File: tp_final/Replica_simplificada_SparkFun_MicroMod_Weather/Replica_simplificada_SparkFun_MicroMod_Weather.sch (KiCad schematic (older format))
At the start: 33 parts, among them J1 USB_C_Receptacle_USB2.0, J2 Conn_01x05, J3 Conn_01x02, J4 Conn_01x03, J5 Conn_01x03, U1 BME280, U2 AP7361C-33F, U3 AS3935

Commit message: PCB revision 1 listo
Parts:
- removed J5: Conn_01x03, Connector_PinSocket_2.54mm:PinSocket_1x03_P2.54mm_Vertical, symbol Connector_Generic:Conn_01x03
- removed U3: AS3935, Package_DFN_QFN:MLPQ-16-1EP_4x4mm_P0.65mm_EP2.8x2.8mm, symbol Sensor:AS3935
- added U3: AS3935, Package_DFN_QFN:MLPQ-16-1EP_4x4mm_P0.65mm_EP2.8x2.8mm, symbol Sensor_lightning:AS3935
- C11: renamed from 0.22u1; value C -> 0.22u
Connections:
- net labels removed: USB_D+, USB_D-, VBUS
- wire segments 121 -> 115
- no-connect marks 7 -> 9
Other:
- moved on the sheet: J3
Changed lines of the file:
@@
 	0    -1   -1   0
-$EndComp
-$Comp
-L Sensor:AS3935 U3
-U 1 1 60618699
-P 3450 3800
-F 0 "U3" H 3450 3900 50  0000 C CNN
-F 1 "AS3935" H 3100 4250 50  0000 C CNN
-F 2 "Package_DFN_QFN:MLPQ-16-1EP_4x4mm_P0.65mm_EP2.8x2.8mm" H 4250 4700 50  0001 C CNN
-F 3 "http://www.embeddedadventures.com/datasheets/AS3935_Datasheet_EN_v2.pdf" H 3350 3800 50  0001 C CNN
-	1    3450 3800
-	1    0    0    -1
 $EndComp
 Text Notes 1200 2500 0    50   ~ 10
 Regulador de tension
 NoConn ~ 4250 8550
-$Comp
-L power:VBUS #PWR021
-U 1 1 6063B3B4
-P 7200 2900
-F 0 "#PWR021" H 7200 2750 50  0001 C CNN
-F 1 "VBUS" H 7215 3073 50  0000 C CNN
-F 2 "" H 7200 2900 50  0001 C CNN
-F 3 "" H 7200 2900 50  0001 C CNN
-	1    7200 2900
-	1    0    0    -1
-$EndComp
 Wire Wire Line
 	7200 2900 7200 2950
@@
 Wire Wire Line
 	7900 3150 7700 3150
-Text GLabel 7100 3650 2    50   BiDi ~ 0
-USB_D+
-Text GLabel 7100 3550 2    50   BiDi ~ 0
-USB_D-
-Wire Wire Line
-	7100 3550 7000 3550
-Wire Wire Line
-	7100 3650 7000 3650
 Wire Notes Line
 	5850 2550 5850 4800
@@
 $EndComp
 $Comp
-L Device:C 0.22u1
+L Device:C C11
 U 1 1 60613459
 P 4200 1250
-F 0 "0.22u1" H 4315 1296 50  0000 L CNN
-F 1 "C" H 4315 1205 50  0000 L CNN
+F 0 "C11" H 4315 1296 50  0000 L CNN
+F 1 "0.22u" H 4315 1205 50  0000 L CNN
 F 2 "Capacitor_SMD:C_1206_3216Metric" H 4238 1100 50  0001 C CNN
 F 3 "~" H 4200 1250 50  0001 C CNN
@@
 F 3 "~" H 5000 3800 50  0001 C CNN
 	1    5000 3800
-	1    0    0    -1
+	1    0    0    1
 $EndComp
 $Comp
@@
 $EndComp
 $Comp
-L Connector_Generic:Conn_01x03 J5
-U 1 1 60825316
-P 8000 4300
-F 0 "J5" H 8080 4342 50  0000 L CNN
-F 1 "Conn_01x03" H 8080 4251 50  0000 L CNN
-F 2 "Connector_PinSocket_2.54mm:PinSocket_1x03_P2.54mm_Vertical" H 8000 4300 50  0001 C CNN
-F 3 "~" H 8000 4300 50  0001 C CNN
-	1    8000 4300
-	1    0    0    -1
-$EndComp
-$Comp
 L Connector_Generic:Conn_01x02 J3
 U 1 1 60825FCB
-P 4100 2150
-F 0 "J3" H 4180 2142 50  0000 L CNN
-F 1 "Conn_01x02" H 4180 2051 50  0000 L CNN
-F 2 "Connector_PinSocket_2.54mm:PinSocket_1x02_P2.54mm_Vertical" H 4100 2150 50  0001 C CNN
-F 3 "~" H 4100 2150 50  0001 C CNN
-	1    4100 2150
-	1    0    0    -1
-$EndComp
-$Comp
-L power:GND #PWR026
-U 1 1 6082664C
-P 7700 4400
-F 0 "#PWR026" H 7700 4150 50  0001 C CNN
-F 1 "GND" H 7705 4227 50  0000 C CNN
-F 2 "" H 7700 4400 50  0001 C CNN
-F 3 "" H 7700 4400 50  0001 C CNN
-	1    7700 4400
+P 4050 2050
+F 0 "J3" H 4130 2042 50  0000 L CNN
+F 1 "Conn_01x02" H 4130 1951 50  0000 L CNN
+F 2 "Connector_PinSocket_2.54mm:PinSocket_1x02_P2.54mm_Vertical" H 4050 2050 50  0001 C CNN
+F 3 "~" H 4050 2050 50  0001 C CNN
+	1    4050 2050
 	1    0    0    -1
 $EndComp
@@
 L power:GND #PWR022
 U 1 1 60826E8D
-P 3800 2250
-F 0 "#PWR022" H 3800 2000 50  0001 C CNN
-F 1 "GND" H 3805 2077 50  0000 C CNN
-F 2 "" H 3800 2250 50  0001 C CNN
-F 3 "" H 3800 2250 50  0001 C CNN
-	1    3800 2250
-	1    0    0    -1
-$EndComp
-Text GLabel 3800 2150 0    50   BiDi ~ 0
+P 3750 2150
+F 0 "#PWR022" H 3750 1900 50  0001 C CNN
+F 1 "GND" H 3755 1977 50  0000 C CNN
+F 2 "" H 3750 2150 50  0001 C CNN
+F 3 "" H 3750 2150 50  0001 C CNN
+	1    3750 2150
+	1    0    0    -1
+$EndComp
+Text GLabel 3750 2050 0    50   BiDi ~ 0
 3.3V_EN
-Text GLabel 7700 4200 0    50   BiDi ~ 0
-USB_D+
-Text GLabel 7700 4300 0    50   BiDi ~ 0
-USB_D-
-Wire Wire Line
-	7700 4300 7800 4300
-Wire Wire Line
-	7700 4200 7800 4200
 Text GLabel 4000 6250 0    50   Input ~ 0
 I2C_SCK
@@
 	4100 6350 4000 6350
 Wire Wire Line
-	3900 2250 3800 2250
-Wire Wire Line
-	3900 2150 3800 2150
-Wire Wire Line
-	7800 4400 7700 4400
+	3850 2150 3750 2150
+Wire Wire Line
+	3850 2050 3750 2050
 $Comp
 L power:PWR_FLAG #FLG01
@@
 Wire Wire Line
 	9850 1050 9850 950
-$Comp
-L power:PWR_FLAG #FLG03
-U 1 1 60868DFA
-P 10700 1050
-F 0 "#FLG03" H 10700 1125 50  0001 C CNN
-F 1 "PWR_FLAG" H 10700 1223 50  0000 C CNN
-F 2 "" H 10700 1050 50  0001 C CNN
-F 3 "~" H 10700 1050 50  0001 C CNN
-	1    10700 1050
-	-1   0    0    1
-$EndComp
-Wire Wire Line
-	10700 950  10700 1050
-$Comp
-L power:VBUS #PWR029
-U 1 1 6086D1A9
-P 10700 950
-F 0 "#PWR029" H 10700 800 50  0001 C CNN
-F 1 "VBUS" H 10715 1123 50  0000 C CNN
-F 2 "" H 10700 950 50  0001 C CNN
-F 3 "" H 10700 950 50  0001 C CNN
-	1    10700 950
-	1    0    0    -1
-$EndComp
 Wire Notes Line
 	8700 4800 8700 2550
@@
 Text Label 4200 3900 0    50   ~ 0
 SPI_SCK
+Text Label 4200 3700 0    50   ~ 0
+SPI_MOSI
 Text Label 4200 3800 0    50   ~ 0
-SPI_MOSI
-Text Label 4200 3700 0    50   ~ 0
 SPI_MISO
 Text Label 4200 3600 0    50   ~ 0
@@
 Wire Notes Line
 	5650 2750 1100 2750
+$Comp
+L power:+5V #PWR0101
+U 1 1 60670ED5
+P 7200 2900
+F 0 "#PWR0101" H 7200 2750 50  0001 C CNN
+F 1 "+5V" H 7215 3073 50  0000 C CNN
+F 2 "" H 7200 2900 50  0001 C CNN
+F 3 "" H 7200 2900 50  0001 C CNN
+	1    7200 2900
+	1    0    0    -1
+$EndComp
+$Comp
+L Sensor_lightning:AS3935 U3
+U 1 1 606F4869
+P 3450 3800
+F 0 "U3" H 3750 4250 50  0000 C CNN
+F 1 "AS3935" H 3100 4250 50  0000 C CNN
+F 2 "Package_DFN_QFN:MLPQ-16-1EP_4x4mm_P0.65mm_EP2.8x2.8mm" H 4250 4700 50  0001 C CNN
+F 3 "https://www.embeddedadventures.com/datasheets/AS3935_Datasheet_EN_v2.pdf" H 3350 3800 50  0001 C CNN
+	1    3450 3800
+	1    0    0    -1
+$EndComp
+NoConn ~ 7000 3550
+NoConn ~ 7000 3650
 $EndSCHEMATC

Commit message: Primeras correciones
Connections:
- net I2C_SCK: now also J4.1 (Pin_1), U1.4 (SCK); no longer J4.2 (Pin_2), U1.3 (SDI)
- net I2C_SDA: now also J4.2 (Pin_2), U1.3 (SDI); no longer J4.1 (Pin_1), U1.4 (SCK)
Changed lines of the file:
@@
 Wire Wire Line
 	2600 6150 2500 6150
-Text GLabel 2600 6150 2    50   Input ~ 0
+Text GLabel 2600 5950 2    50   Input ~ 0
 I2C_SCK
-Text GLabel 2600 5950 2    50   BiDi ~ 0
+Text GLabel 2600 6150 2    50   BiDi ~ 0
 I2C_SDA
 Wire Wire Line
@@
 Text GLabel 3750 2050 0    50   BiDi ~ 0
 3.3V_EN
-Text GLabel 4000 6250 0    50   Input ~ 0
+Text GLabel 4000 6150 0    50   Input ~ 0
 I2C_SCK
-Text GLabel 4000 6150 0    50   BiDi ~ 0
+Text GLabel 4000 6250 0    50   BiDi ~ 0
 I2C_SDA
 Wire Wire Line

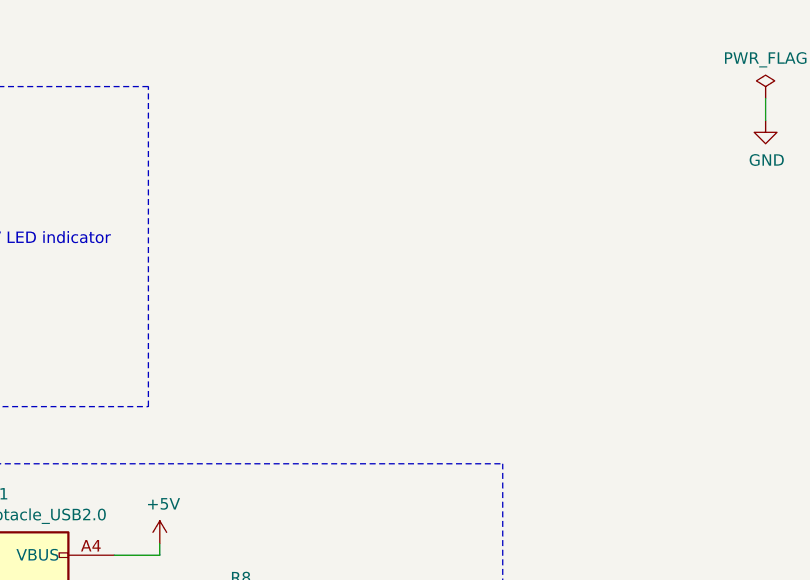
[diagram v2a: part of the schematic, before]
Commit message: Agrego mounting hole y fiduciales al esquematico
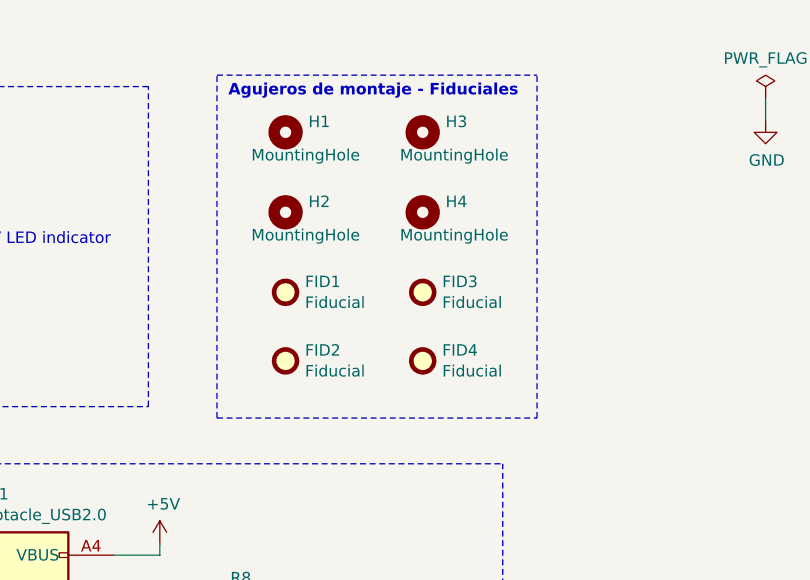
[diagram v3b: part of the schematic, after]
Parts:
- added FID1, FID2, FID3, FID4: Fiducial, Fiducial:Fiducial_0.5mm_Mask1.5mm, symbol Mechanical:Fiducial
- added H1, H2, H3, H4: MountingHole, MountingHole:MountingHole_2.2mm_M2_ISO7380, symbol Mechanical:MountingHole
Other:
- note added: "Agujeros de montaje - Fiduciales"
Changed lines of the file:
@@
 NoConn ~ 7000 3550
 NoConn ~ 7000 3650
+$Comp
+L Mechanical:MountingHole H1
+U 1 1 606FE880
+P 7750 1100
+F 0 "H1" H 7850 1146 50  0000 L CNN
+F 1 "MountingHole" H 7600 1000 50  0000 L CNN
+F 2 "MountingHole:MountingHole_2.2mm_M2_ISO7380" H 7750 1100 50  0001 C CNN
+F 3 "~" H 7750 1100 50  0001 C CNN
+	1    7750 1100
+	1    0    0    -1
+$EndComp
+$Comp
+L Mechanical:MountingHole H3
+U 1 1 606FFEA2
+P 8350 1100
+F 0 "H3" H 8450 1146 50  0000 L CNN
+F 1 "MountingHole" H 8250 1000 50  0000 L CNN
+F 2 "MountingHole:MountingHole_2.2mm_M2_ISO7380" H 8350 1100 50  0001 C CNN
+F 3 "~" H 8350 1100 50  0001 C CNN
+	1    8350 1100
+	1    0    0    -1
+$EndComp
+$Comp
+L Mechanical:MountingHole H2
+U 1 1 6070009E
+P 7750 1450
+F 0 "H2" H 7850 1496 50  0000 L CNN
+F 1 "MountingHole" H 7600 1350 50  0000 L CNN
+F 2 "MountingHole:MountingHole_2.2mm_M2_ISO7380" H 7750 1450 50  0001 C CNN
+F 3 "~" H 7750 1450 50  0001 C CNN
+	1    7750 1450
+	1    0    0    -1
+$EndComp
+$Comp
+L Mechanical:MountingHole H4
+U 1 1 607007D6
+P 8350 1450
+F 0 "H4" H 8450 1496 50  0000 L CNN
+F 1 "MountingHole" H 8250 1350 50  0000 L CNN
+F 2 "MountingHole:MountingHole_2.2mm_M2_ISO7380" H 8350 1450 50  0001 C CNN
+F 3 "~" H 8350 1450 50  0001 C CNN
+	1    8350 1450
+	1    0    0    -1
+$EndComp
+$Comp
+L Mechanical:Fiducial FID1
+U 1 1 6070160A
+P 7750 1800
+F 0 "FID1" H 7835 1846 50  0000 L CNN
+F 1 "Fiducial" H 7835 1755 50  0000 L CNN
+F 2 "Fiducial:Fiducial_0.5mm_Mask1.5mm" H 7750 1800 50  0001 C CNN
+F 3 "~" H 7750 1800 50  0001 C CNN
+	1    7750 1800
+	1    0    0    -1
+$EndComp
+$Comp
+L Mechanical:Fiducial FID3
+U 1 1 60701BC5
+P 8350 1800
+F 0 "FID3" H 8435 1846 50  0000 L CNN
+F 1 "Fiducial" H 8435 1755 50  0000 L CNN
+F 2 "Fiducial:Fiducial_0.5mm_Mask1.5mm" H 8350 1800 50  0001 C CNN
+F 3 "~" H 8350 1800 50  0001 C CNN
+	1    8350 1800
+	1    0    0    -1
+$EndComp
+$Comp
+L Mechanical:Fiducial FID2
+U 1 1 607021A7
+P 7750 2100
+F 0 "FID2" H 7835 2146 50  0000 L CNN
+F 1 "Fiducial" H 7835 2055 50  0000 L CNN
+F 2 "Fiducial:Fiducial_0.5mm_Mask1.5mm" H 7750 2100 50  0001 C CNN
+F 3 "~" H 7750 2100 50  0001 C CNN
+	1    7750 2100
+	1    0    0    -1
+$EndComp
+$Comp
+L Mechanical:Fiducial FID4
+U 1 1 6070274C
+P 8350 2100
+F 0 "FID4" H 8435 2146 50  0000 L CNN
+F 1 "Fiducial" H 8435 2055 50  0000 L CNN
+F 2 "Fiducial:Fiducial_0.5mm_Mask1.5mm" H 8350 2100 50  0001 C CNN
+F 3 "~" H 8350 2100 50  0001 C CNN
+	1    8350 2100
+	1    0    0    -1
+$EndComp
+Wire Notes Line
+	8850 2350 8850 850
+Text Notes 7500 950  0    50   ~ 10
+Agujeros de montaje - Fiduciales
+Wire Notes Line
+	7450 2350 7450 850
+Wire Notes Line
+	7450 2350 8850 2350
+Wire Notes Line
+	7450 850  8850 850
 $EndSCHEMATC

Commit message: Correciones finales
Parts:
- removed C2: 10u, Capacitor_SMD:C_1206_3216Metric, symbol Device:C
- C1, C9: value 10u -> 10uF
- C10, C8: value 1u -> 1uF
- C11, C3: value 0.22u -> 0.22uF
- C4, C7: value 0.1u -> 0.1uF
- C6: value 1n -> 1nC
- D1: footprint Diode_SMD:D_TUMD2 -> Diode_SMD:D_SOD-123F; Código de digikey (none) -> RB070MM-30TR-ND; Código de fabricante (none) -> RB070MM-30TR; Fabricante (none) -> Rohm Semiconductor
- J1: Código de Digikey (none) -> WM11263TR-ND; Código de fabricante (none) -> 1051640001; Fabricante (none) -> Molex
- L1: value 100u -> 100uH; Código de Digikey (none) -> A102544TR-ND; Código de fabricante (none) -> 3613C101K; Fabricante (none) -> TE Connectivity Passive Product
- U1: Código de Digikey (none) -> 828-1063-2-ND; Código del fabricante (none) -> BME280; Fabricante (none) -> Bosch Sensortec
- U2: Código de Digikey (none) -> AP7361C-33FGE-7DITR-ND; Código del fabricante (none) -> AP7361C-33FGE-7; Fabricante (none) -> Diodes Incorporated
- U3: Código de Digikey (none) -> AS3935-BQFTTR-ND; Código del fabricante (none) -> AS3935-BQFT; Fabricante (none) -> ScioSense
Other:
- note added: "USB - Alimentación"
- note removed: "USB"
- moved on the sheet: C1, C10, C11, C3, C4, C5, C6, C7, C8, C9, D1, D2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
